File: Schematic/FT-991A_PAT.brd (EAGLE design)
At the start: 44.6 x 59.8 mm, 69 parts, among them Q1 PE4259, Q2 PE4259, Q3 J310, Q4 BD90GA5WEFJ, Q5 PE4259, Q6 PE4259, Q7 MC78M05CDTRKG, Q8 MIC5365-3.3, Q9 PE4259, T1 BFS17, U1 SN74AHC1G08_DCK_5, X1 IF_IN, X2 SCP_OUT, X3 87583-3010RPALF, X4 SDR_OUT

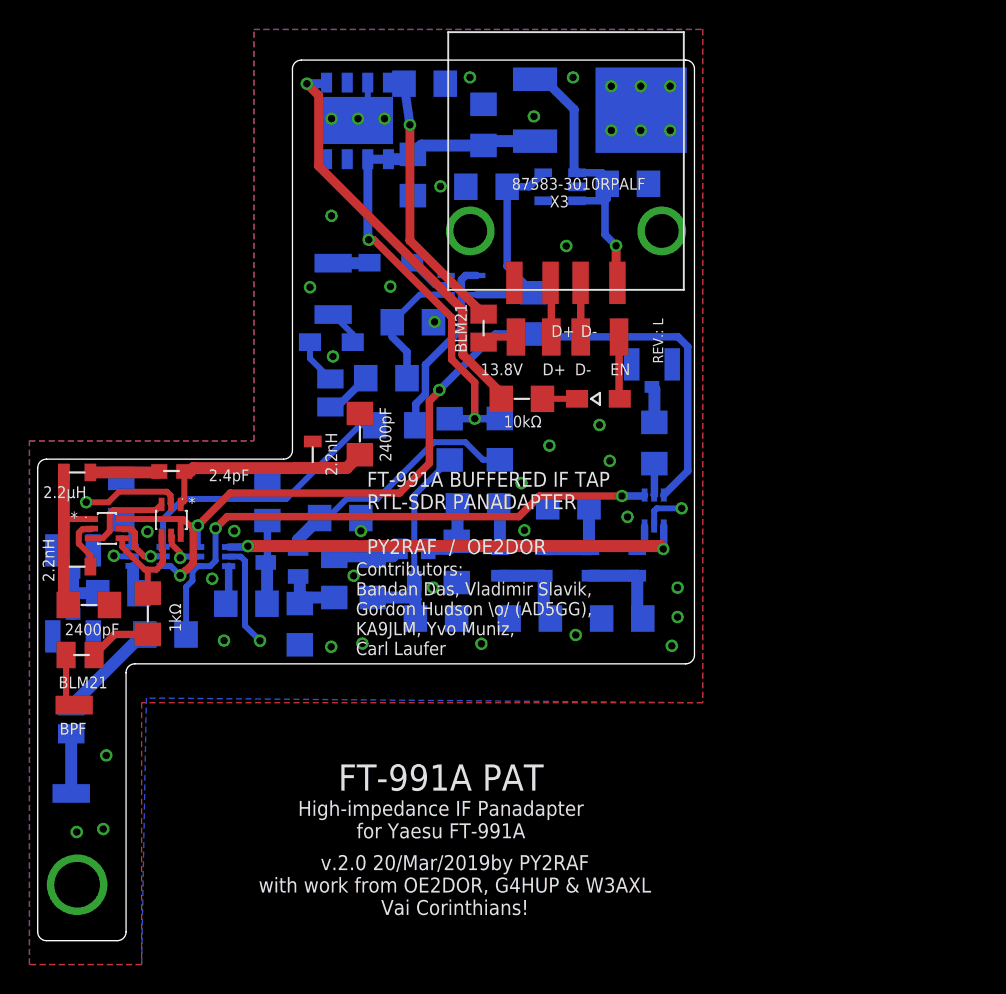
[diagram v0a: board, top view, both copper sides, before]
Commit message: Revision M
In this revision:
* Got rid of the USB receptacle - Too much space in a tight radio
* Moved all GPIO pads to the upper board side
* Added a few missing Pin 1 references
* Renamed voltage regulators to somewhat shorter name
* Small re-routing - 9V regulator was entangled with capacitor
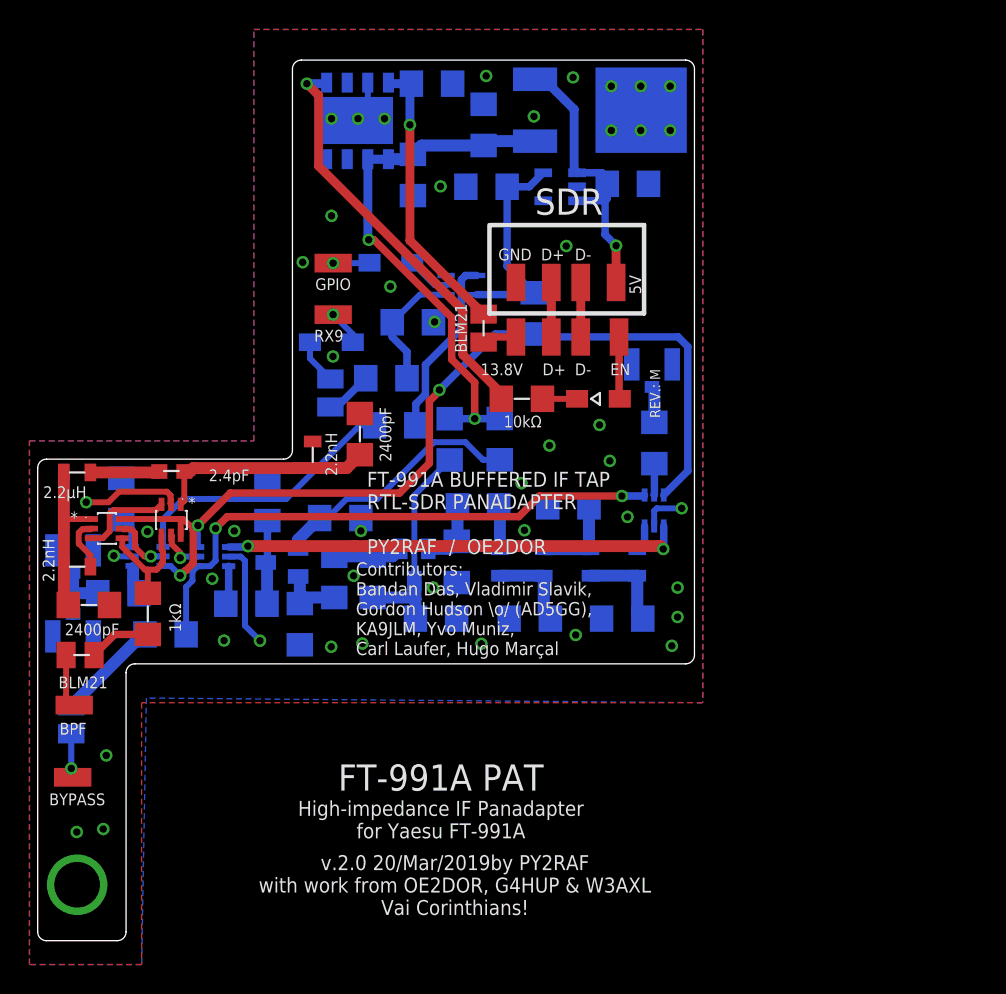
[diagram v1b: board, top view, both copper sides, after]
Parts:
- removed X3: 87583-3010RPALF, psemi:USB-SMD-AMP
- added PAD10: D-, wirepad:SMD1,27-2,54
- added PAD11: D+, wirepad:SMD1,27-2,54
- added PAD12: GND, wirepad:SMD1,27-2,54
- added PAD9: 5V, wirepad:SMD1,27-2,54
- Q8: value MIC5365-3.3 -> MIC5365-3.3
- moved PAD6 1.10 mm to (8.70, 22.7), flipped to the top
- moved C5 0.50 mm to (33.1, 69.8)
- flipped PAD2 to the top
- flipped PAD3 to the top
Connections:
- net GNDA: now also PAD12.1; no longer X3.5, X3.6, X3.GND
- net N$25: now also PAD10.1; no longer X3.D-
- net N$33: now also PAD11.1; no longer X3.D+
- net N$34: now also PAD9.1; no longer X3.VCC
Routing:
- net N$41: track 4.05 -> 2.99 mm, vias 0 -> 1
- net N$18: vias 0 -> 1
- net N$16: vias 0 -> 1
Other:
- board text added: "5V"
- board text added: "Contributors: Bandan Das, Vladimir Slavik, Gordon Hudson \\o/ (AD5GG), KA9JLM, Yvo Muniz, Carl Laufer, Hugo Marçal"
- board text added: "GND"
- board text added: "REG3.3V"
- board text added: "REG5V"
- board text added: "REG9V"
- board text added: "REV.: M"
- board text added: "SDR"
- board text removed: "Contributors: Bandan Das, Vladimir Slavik, Gordon Hudson \\o/ (AD5GG), KA9JLM, Yvo Muniz, Carl Laufer"
- board text removed: "REV.: L"

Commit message: Revision N - No USB
A truckload of changes. Namely:
* Removed the 5V regulator
* Removed the USB provisions
* Removed the G4HUP LPF. Reasoning: Found it of no use, since it cuts
* the signal 24 MHz above the IF center frequency. The selectable BPF
* suits better.
* Moved regulators to the top side of the board (to take advantage of
* heat dissipation)
* Moved the SDR Out port to the top of the board
* Added a large uncovered ground pad
* Tried to group the signals as much as possible and moved everything to
* the top of the board
* And thus, reduced significantly the BOM (35 to 25 different parts)
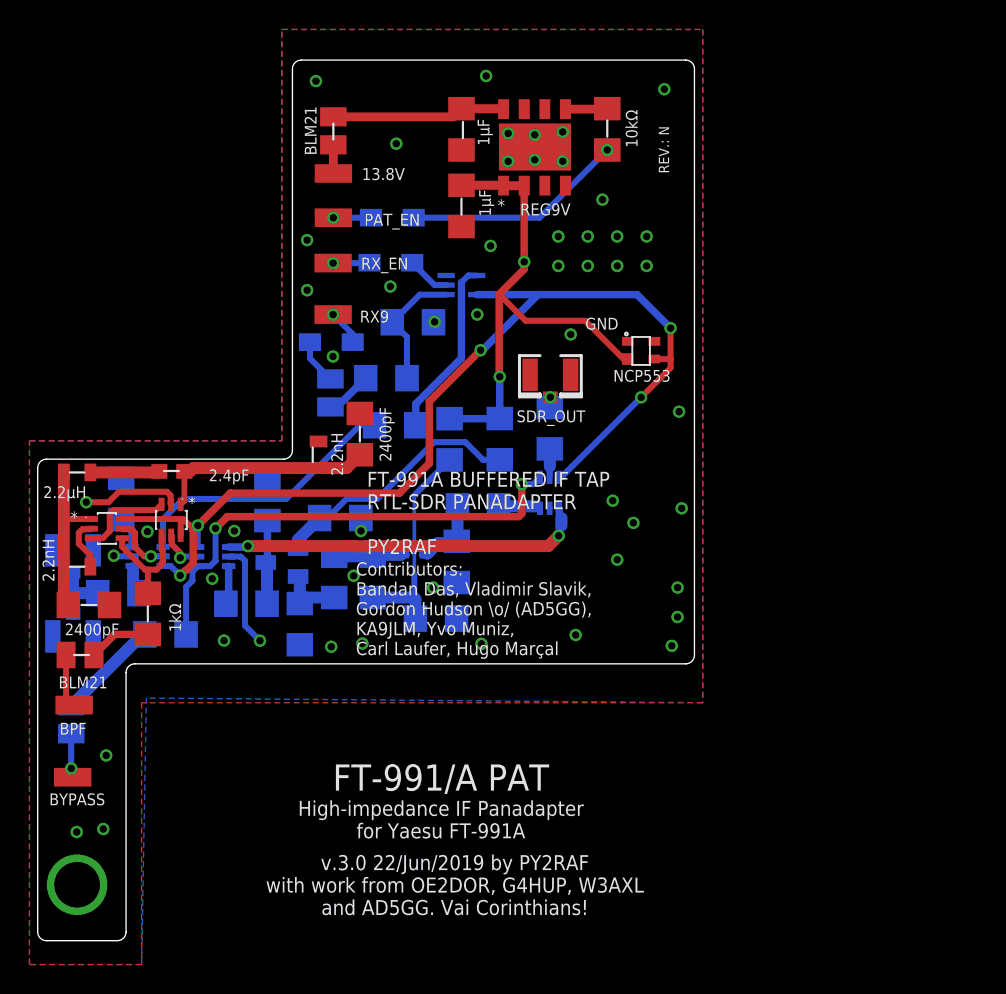
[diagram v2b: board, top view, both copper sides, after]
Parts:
- removed C14, C17: 1µF, rcl:C3216
- removed C15, C18: 56pF, rcl:C3216
- removed C16: 68pF, rcl:C3216
- removed C19: 1nF, rcl:C3216
- removed L10, L8: 180nH, aarf:0805
- removed L11: 82nH, aarf:0805
- removed L9: BLM21, rcl-modified:L0805
- removed PAD10, PAD7: D-, wirepad:SMD1,27-2,54
- removed PAD11, PAD8: D+, wirepad:SMD1,27-2,54
- removed PAD12: GND, wirepad:SMD1,27-2,54
- removed PAD9: 5V, wirepad:SMD1,27-2,54
- removed R13: 1kΩ, rcl:R3216
- removed T1: BFS17, transistor:SOT23
- removed U1: SN74AHC1G08_DCK_5, sn74ahc1g08-dck:DCK5
- removed X4: SDR_OUT, adafruit:U.FL
- added Q10: PE4259, aarf:SC-70
- added X3: SDR_OUT, adafruit:U.FL
- C13: value 0.33µF -> 1nF
- L7: value 82nH -> BLM21; device aarf:0805 -> rcl-modified:L0805
- PAD2: value GPIO -> RX_EN
- PAD5: value EN -> PAT_EN
- Q1: value PE4259 -> SN74AHC1G08; device aarf:SC-70 -> aarf:DCK5
- Q3: value J310 -> NCP553; device transistor-fet:SOT23 -> aarf:SC-82AB
- Q4: value BD90GA5WEFJ -> PE4259; device aarf:HTSOP-J8 -> aarf:SC-70
- Q5: value PE4259 -> J310; device aarf:SC-70 -> transistor-fet:SOT23
- Q6: value PE4259 -> BD90GA5WEFJ; device aarf:SC-70 -> aarf:HTSOP-J8
- Q7: value MC78M05CDTRKG -> 2SC5086; device aarf:DPAK-3 -> aarf:2-2H1A
- Q8: value MIC5365-3.3 -> PE4259; device aarf:SOT23-5L -> aarf:SC-70
- R1: value 2k8Ω -> 10kΩ
- R10: value 39kΩ -> 1kΩ
- R11: value 1kΩ -> 100Ω
- R12: value 100Ω -> 1kΩ
- R3: value 1k62Ω -> 5.6kΩ
- R5: value 1kΩ -> 100kΩ
- R6: value 100kΩ -> 1kΩ
- R7: value 1kΩ -> 220Ω
- R8: value 220Ω -> 1kΩ
- R9: value 1kΩ -> 39kΩ
- moved Q6 35.3 mm to (40.1, 65.4), turned to 90 degrees
- moved Q8 34.4 mm to (18.3, 37.7)
- moved Q7 33.0 mm to (31.9, 37.1)
- moved Q9 32.8 mm to (15.4, 40.2), flipped to the top, turned to 180 degrees
- moved Q4 32.8 mm to (13.8, 37.7)
- moved L7 31.0 mm to (8.60, 26.6)
- moved Q1 29.2 mm to (35.1, 56.1), flipped to the bottom, turned to 180 degrees
- moved Q3 28.3 mm to (47.3, 51.7), flipped to the top
- moved R5 22.1 mm to (21.9, 41.5), turned to 270 degrees
- moved C13 21.1 mm to (41.1, 46.4)
- moved PAD5 21.0 mm to (26.4, 60.7), turned to 90 degrees
- moved R12 20.4 mm to (15.0, 32.4), turned to 0 degrees
- moved R4 19.2 mm to (45.0, 66.7), turned to 90 degrees
- moved D3 18.6 mm to (30.4, 60.7), flipped to the bottom
- moved R8 18.5 mm to (24.1, 33.1)
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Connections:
- removed net N$11: C16.1, L10.P$1, L8.P$2
- removed net N$13: C18.1, L10.P$2, L11.P$1
- removed net N$15: L11.P$2, Q9.3
- removed net N$17: R1.1, R3.1, U1.1
- removed net N$25: PAD10.1, PAD7.1
- removed net N$3: C15.1, L7.P$2, L8.P$1
- removed net N$33: PAD11.1, PAD8.1
- removed net N$34: C17.1, PAD9.1, Q7.P$3, Q8.1, Q8.3
- net GNDA: now also Q1.3, Q10.2, Q3.1, Q4.2, Q6.P$3, Q6.P$4, Q6.P$6, Q6.P$7, Q6.P$9, R11.2, R5.1, R8.1, X3.1, X3.2; no longer C13.2, C14.2, C15.2, C16.2, C17.2, C18.2, PAD12.1, Q1.2, Q4.P$3, Q4.P$4, Q4.P$6, Q4.P$7, Q4.P$9, Q5.2, Q6.2, Q7.P$2, R12.2, R6.1, R9.1, U1.3, X4.1, X4.2
- net N$1: now also Q7.2, R11.1; no longer R12.1, T1.2
- net N$10: now also Q7.3, R10.2, R9.1; no longer R10.1, R11.2, T1.3
- net N$12: now also Q8.3; no longer Q5.3
- net N$19: now also Q4.4, R6.2; no longer Q2.4, R7.2
- net N$2: now also Q10.3; no longer L7.P$1
- net N$20: now also Q1.2; no longer U1.2
- net N$21: now also Q4.1; no longer Q2.1
- net N$22: now also Q1.4, R6.1; no longer R7.1, U1.4
- net N$23: now also L7.1, R12.2; no longer L9.1, R13.2
- net N$24: now also Q4.3; no longer Q2.3
- net N$26: now also Q6.P$8; no longer Q4.P$8
- net N$31: now also Q6.P$5; no longer Q4.P$5
- net N$37: now also C13.2, X3.3; no longer C19.2, X4.3
- net N$38: now also Q10.1, Q8.1; no longer Q5.1, Q9.1
- net N$39: now also C13.1, Q10.5; no longer C19.1, Q9.5
- net N$4: now also Q7.1, R9.2; no longer R10.2, T1.1
- net N$40: now also Q10.4, Q8.4, R12.1; no longer Q5.4, Q9.4, R13.1
- net N$41: now also L7.2; no longer L9.2
- net N$43: now also Q9.1; no longer Q6.1
- net N$46: now also Q2.4, Q9.4; no longer Q1.4, Q6.4
- net N$47: now also Q4.5; no longer Q1.5
- net N$48: now also Q2.3, Q9.3; no longer Q1.3, Q6.3
- net N$49: now also Q8.5, Q9.5; no longer Q5.5, Q6.5
- net N$5: now also Q5.2, R8.2; no longer Q3.2, R9.2
- net N$6: now also Q5.3, R5.2; no longer Q3.3, R6.2
- net N$7: now also Q2.1; no longer Q1.1
- net N$8: now also Q1.1, R1.1, R3.1; no longer C10.1, C13.1, Q4.P$1, Q4.P$2, Q7.P$1, R11.1, R8.2
- net N$9: now also Q5.1, R7.1; no longer Q3.1, R8.1
- net VCC: now also C10.1, Q3.2, Q6.P$1, Q6.P$2, R10.1, R7.2; no longer C14.1, Q8.5, R5.2, U1.5
- net VDD: now also Q1.5, Q10.6, Q3.3, Q4.6, Q8.6; no longer Q1.6, Q5.6, Q6.6, R5.1
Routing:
- net N$8: track 36.1 -> 8.65 mm, vias 2 -> 0
- net N$31: track 28.2 -> 2.85 mm, vias 1 -> 0
- net VCC: track 14.7 -> 34.8 mm, vias 0 -> 2
- net N$34: track 19.4 -> 0.00 mm, vias 1 -> 0
- net N$30: track 2.35 -> 15.1 mm, vias 0 -> 1
- net VDD: track 65.6 -> 73.9 mm, vias 3 -> 5
- net N$26: track 19.4 -> 11.8 mm, vias 1 -> 0
- net N$17: track 8.65 -> 1.59 mm
- net N$38: track 31.2 -> 24.6 mm
- net GNDA: track 24.5 -> 18.7 mm, vias 47 -> 53
- net N$13: track 6.24 -> 0.50 mm
- net N$40: track 38.6 -> 33.2 mm
- net N$11: track 6.13 -> 1.10 mm
- net N$3: track 6.07 -> 2.10 mm
- net N$33: track 3.70 -> 0.00 mm
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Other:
- board text added: "5086"
- board text added: "AND"
- board text added: "FT-991/A PAT"
- board text added: "FT-991A BUFFERED IF TAP RTL-SDR PANADAPTER PY2RAF"
- board text added: "PAT_EN"
- board text added: "REV.: N"
- board text added: "v.3.0 22/Jun/2019 by PY2RAF with work from OE2DOR, G4HUP, W3AXL and AD5GG. Vai Corinthians!"
- board text removed: "5V"
- board text removed: "D+"
- board text removed: "D-"
- board text removed: "EN"
- board text removed: "FT-991A BUFFERED IF TAP RTL-SDR PANADAPTER PY2RAF / OE2DOR"
- board text removed: "FT-991A PAT"
- board text removed: "REG3.3V"
- board text removed: "REG5V"
- board text removed: "REV.: M"
- board text removed: "SDR"
- board text removed: "v.2.0 20/Mar/2019by PY2RAF with work from OE2DOR, G4HUP & W3AXL Vai Corinthians!"

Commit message: Starting Revision O Redesign
Still preliminary, a lot more work to do.
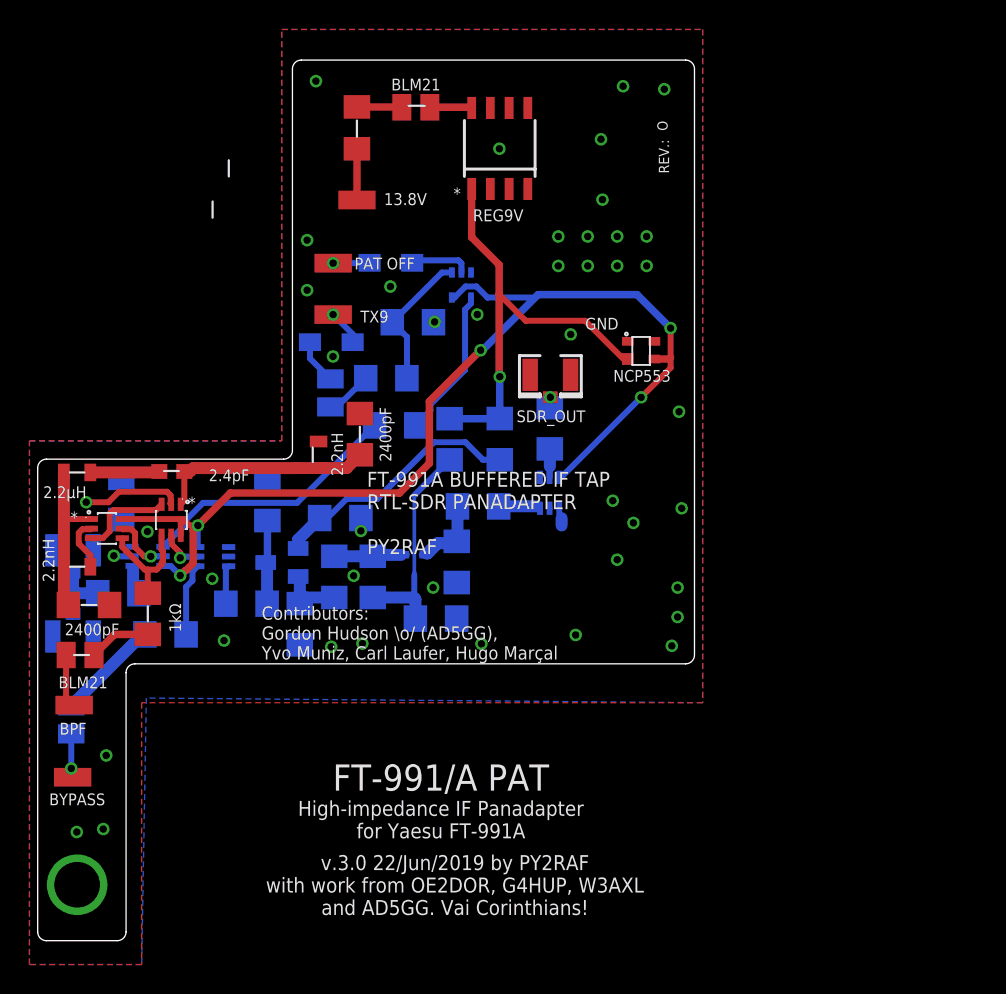
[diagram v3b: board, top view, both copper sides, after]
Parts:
- removed C10, C5: 1µF, rcl:C3216
- removed D3: 1SS355VM, diode:SOD323-W
- removed PAD5: PAT_EN, wirepad:SMD1,27-2,54
- removed R4: 10kΩ, rcl:R3216
- added F1: 150 mA, adafruit:R1206
- PAD2: value RX_EN -> PAT OFF
- PAD3: value RX9 -> TX9
- Q1: value SN74AHC1G08 -> SN74AHC-OR; device aarf:DCK5 -> aarf:SC70-5
- Q6: value BD90GA5WEFJ -> MC78L09ABDR2GOSCT; device aarf:HTSOP-J8 -> aarf:SOIC8
- moved L3 5.82 mm to (32.0, 68.2), turned to 180 degrees
- moved PAD4 2.41 mm to (28.0, 61.9)
- moved Q6 2.40 mm to (37.7, 65.4), turned to 0 degrees
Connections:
- removed net N$29 (its old number): D3.A, PAD5.1
- removed net N$30: D3.C, R4.1
- removed net N$31: Q6.P$5, R4.2
- new net N$32: F1.2, L3.2
- net GNDA: now also Q6.2, Q6.3, Q6.6, Q6.7; no longer C10.2, C5.2, Q6.P$3, Q6.P$4, Q6.P$6, Q6.P$7, Q6.P$9
- net N$21: now also C2.2; no longer C1.2
- net N$24: now also C1.2; no longer C2.2
- net N$26: now also Q6.8; no longer C5.1, Q6.P$8
- net N$28: now also F1.1; no longer L3.2
- net VCC: now also Q6.1; no longer C10.1, Q6.P$1, Q6.P$2
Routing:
- net N$40: track 33.2 -> 4.96 mm, vias 2 -> 0
- net N$33: track 24.6 -> 0.00 mm, vias 2 -> 0
- net N$30: track 15.1 -> 0.00 mm, vias 1 -> 0
- net N$26: track 11.8 -> 2.87 mm
- net GNDA: track 18.7 -> 11.6 mm, vias 53 -> 45
- net VCC: track 34.8 -> 30.1 mm, vias 2 -> 1
- net N$32: track 0.00 -> 3.06 mm
- net N$31: track 2.85 -> 0.00 mm
- net N$29 (its old number): track 2.55 -> 0.00 mm, vias 1 -> 0
- net VDD: track 73.9 -> 76.2 mm
- net N$24: track 2.15 -> 0.00 mm
- net N$21: track 2.05 -> 0.00 mm
- net N$22: track 12.2 -> 10.2 mm
- net N$28: track 1.95 -> 3.48 mm
- net N$20: track 2.93 -> 4.12 mm
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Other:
- board text added: ">REVISION_ID"
- board text added: "Contributors: Gordon Hudson \\o/ (AD5GG), Yvo Muniz, Carl Laufer, Hugo Marçal"
- board text added: "REV.:"
- board text removed: "Contributors: Bandan Das, Vladimir Slavik, Gordon Hudson \\o/ (AD5GG), KA9JLM, Yvo Muniz, Carl Laufer, Hugo Marçal"
- board text removed: "PAT_EN"
- board text removed: "REV.: N"
